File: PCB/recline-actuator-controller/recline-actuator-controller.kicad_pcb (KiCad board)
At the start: 4 copper layers, 140 x 100 mm, 130 parts, among them J1 DX07S016JA1R1500, J10 1757242, J11 1757242, J12 0705530002, J13 0705530002, J14 0705530002, J15 0705530002, J2 Conn_01x03, J3 RJHSE-5381, J4 1757242, J5 1757242, J6 1757242, J7 1757242, J8 1757242, J9 1757242, M1 D24V22F5, M2 D24V22F3, Q1 PSMN7R0-60YS,115, Q2 PSMN7R0-60YS,115, Q3 PSMN7R0-60YS,115, Q4 PSMN7R0-60YS,115, Q5 PSMN7R0-60YS,115, Q6 BSC014N04LSIATMA1, Q7 BSC014N04LSIATMA1, SW1 TL3330AF260QG, SW2 TL3330AF260QG, U1 TEMPLATE, U2 RP2040, U3 MAX3535ECWI+T, U4 VNH5019ATR-E, U5 VNH5019ATR-E, X1 ABM8G-12.000MHZ-18-D2Y-T

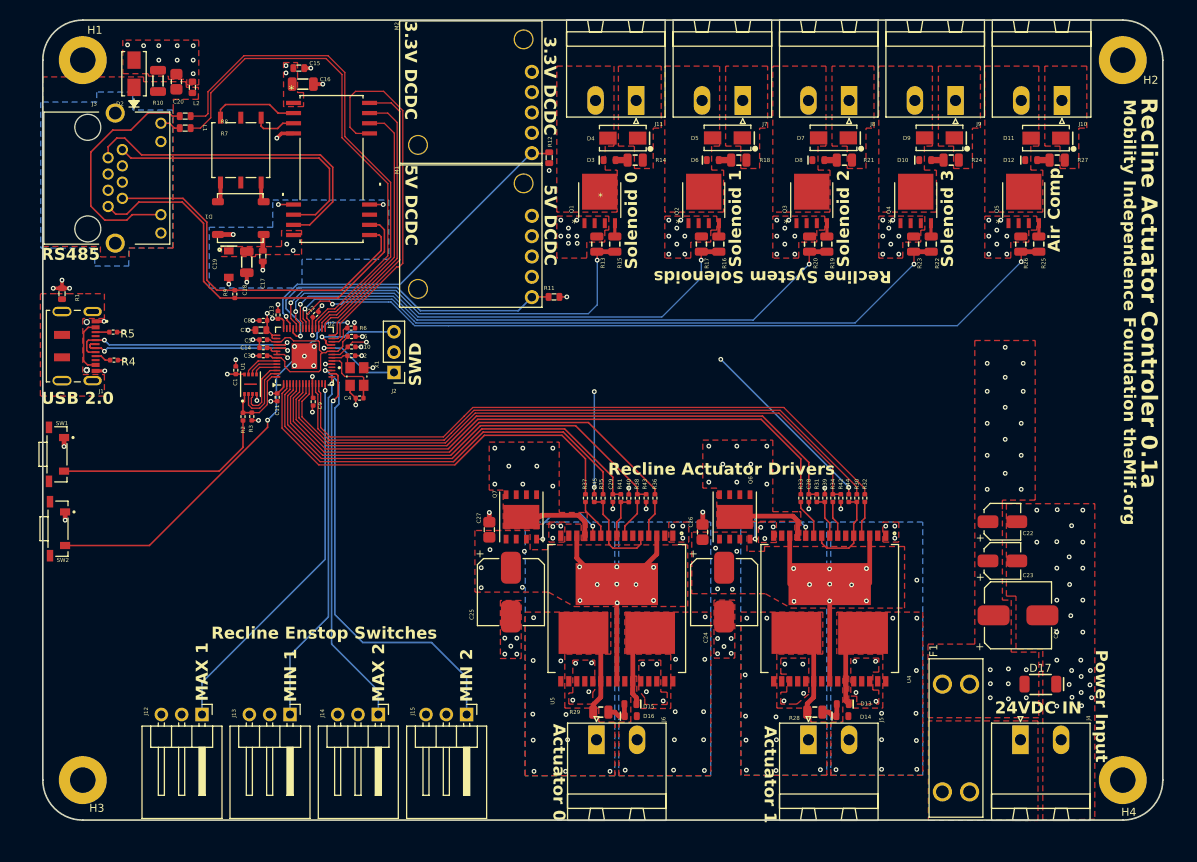
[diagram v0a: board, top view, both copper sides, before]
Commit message: More Motor Channels
Adding more motor channels to actuator control board it will need new MCU or port expansion.
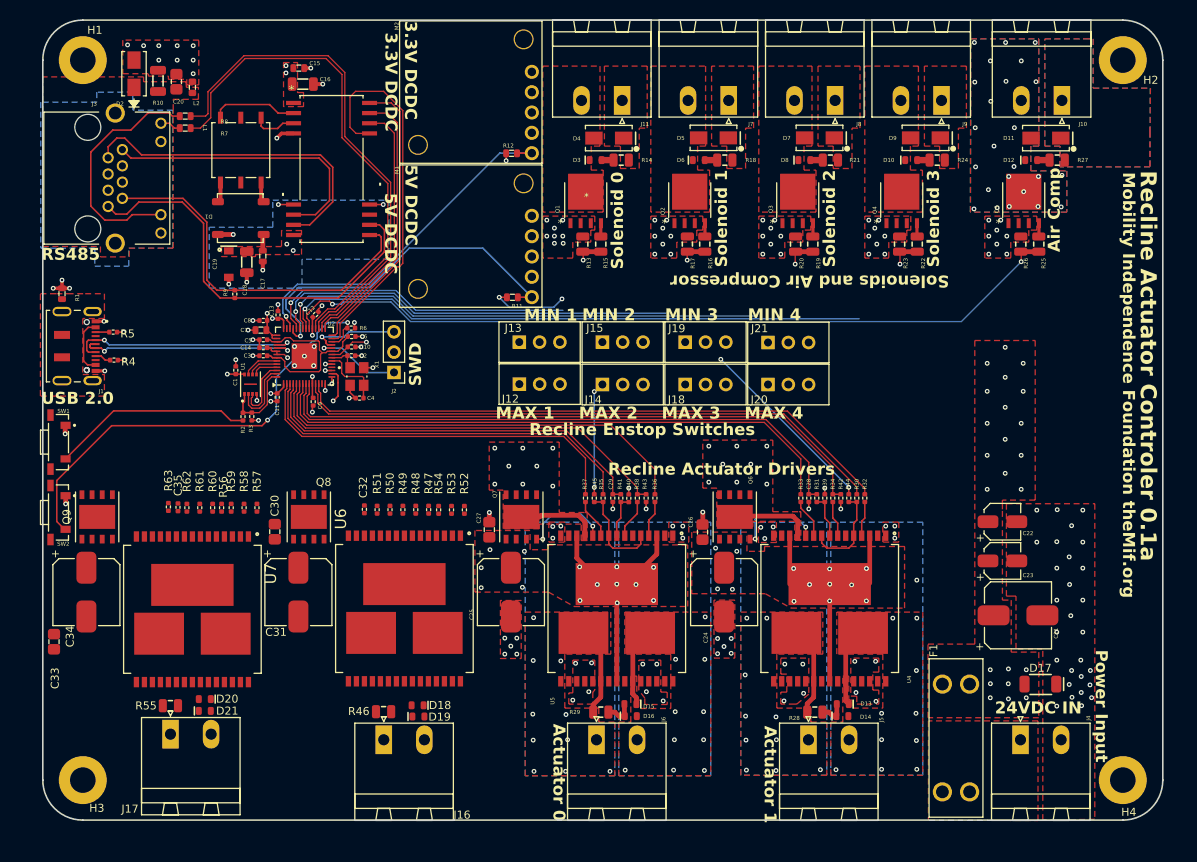
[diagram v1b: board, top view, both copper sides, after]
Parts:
- added C30: CL21B104KBFNNNE, AVR-KiCAD-Lib-Capacitors:C0805, F.Cu at (79.0, 109.0)
- added C31: UUQ1H470MCL1GS, AVR-KiCAD-Lib-Capacitors:CP_Elec_8x10, F.Cu at (82.0, 116.5)
- added C32: C0402C333K4REC7867, AVR-KiCAD-Lib-Capacitors:C0402, F.Cu at (90.2, 106.2)
- added C33: CL21B104KBFNNNE, AVR-KiCAD-Lib-Capacitors:C0805, F.Cu at (51.4, 122.7)
- added C34: UUQ1H470MCL1GS, AVR-KiCAD-Lib-Capacitors:CP_Elec_8x10, F.Cu at (55.5, 116.5)
- added C35: C0402C333K4REC7867, AVR-KiCAD-Lib-Capacitors:C0402, F.Cu at (66.9, 105.9)
- added D18: LTST-C194KGKT, AVR-KiCAD-Lib-Diodes:LED0603, F.Cu at (96.8, 130.7)
- added D19: LTST-C194TBKT, AVR-KiCAD-Lib-Diodes:LED0603, F.Cu at (97.0, 132.1)
- added D20: LTST-C194KGKT, AVR-KiCAD-Lib-Diodes:LED0603, F.Cu at (70.2, 129.9)
- added D21: LTST-C194TBKT, AVR-KiCAD-Lib-Diodes:LED0603, F.Cu at (70.2, 131.3)
- added J16: 1757242, AVR-KiCAD-Lib-Connectors:PhoenixContact_MSTBA-G_02x5.08mm_Angled, F.Cu at (92.6, 135.0)
- added J17: 1757242, AVR-KiCAD-Lib-Connectors:PhoenixContact_MSTBA-G_02x5.08mm_Angled, F.Cu at (66.0, 134.3)
- added J18: 0705430002, AVR-KiCAD-Lib-Connectors:Shrouded_Pin_Header_Straight_1x03_Pitch2.54mm, F.Cu at (130.3, 90.5)
- added J19: 0705430002, AVR-KiCAD-Lib-Connectors:Shrouded_Pin_Header_Straight_1x03_Pitch2.54mm, F.Cu at (130.3, 85.2)
- added J20: 0705430002, AVR-KiCAD-Lib-Connectors:Shrouded_Pin_Header_Straight_1x03_Pitch2.54mm, F.Cu at (140.7, 90.5)
- added J21: 0705430002, AVR-KiCAD-Lib-Connectors:Shrouded_Pin_Header_Straight_1x03_Pitch2.54mm, F.Cu at (140.7, 85.3)
- added Q8: BSC014N04LSIATMA1, AVR-KiCAD-Lib-Transistors:PG-TDSON-8_INF, F.Cu at (83.3, 107.1)
- added Q9: BSC014N04LSIATMA1, AVR-KiCAD-Lib-Transistors:PG-TDSON-8_INF, F.Cu at (56.8, 107.1)
- added R46: RC0805FR-074K7L, AVR-KiCAD-Lib-Resistors:R0805, F.Cu at (92.6, 131.4)
- added R47: RC0402FR-074K7L, AVR-KiCAD-Lib-Resistors:R0402, F.Cu at (98.2, 106.2)
- added R48: RC0402FR-071KL, AVR-KiCAD-Lib-Resistors:R0402, F.Cu at (96.6, 106.2)
- added R49: RC0402FR-071KL, AVR-KiCAD-Lib-Resistors:R0402, F.Cu at (95.0, 106.2)
- added R50: RC0402FR-071KL, AVR-KiCAD-Lib-Resistors:R0402, F.Cu at (93.4, 106.2)
- added R51: RC0402FR-071KL, AVR-KiCAD-Lib-Resistors:R0402, F.Cu at (91.8, 106.2)
- added R52: RC0402FR-071KL, AVR-KiCAD-Lib-Resistors:R0402, F.Cu at (102.7, 106.2)
- added R53: RC0402FR-0710KL, AVR-KiCAD-Lib-Resistors:R0402, F.Cu at (101.1, 106.2)
- added R54: RC0402FR-0710KL, AVR-KiCAD-Lib-Resistors:R0402, F.Cu at (99.5, 106.2)
- added R55: RC0805FR-074K7L, AVR-KiCAD-Lib-Resistors:R0805, F.Cu at (66.0, 130.7)
- added R56: RC0402FR-074K7L, AVR-KiCAD-Lib-Resistors:R0402, F.Cu at (72.3, 106.0)
- added R57: RC0402FR-071KL, AVR-KiCAD-Lib-Resistors:R0402, F.Cu at (76.8, 106.0)
- added R58: RC0402FR-071KL, AVR-KiCAD-Lib-Resistors:R0402, F.Cu at (75.2, 106.0)
- added R59: RC0402FR-071KL, AVR-KiCAD-Lib-Resistors:R0402, F.Cu at (73.5, 106.0)
- added R60: RC0402FR-071KL, AVR-KiCAD-Lib-Resistors:R0402, F.Cu at (71.2, 106.0)
- added R61: RC0402FR-071KL, AVR-KiCAD-Lib-Resistors:R0402, F.Cu at (69.6, 106.0)
- added R62: RC0402FR-0710KL, AVR-KiCAD-Lib-Resistors:R0402, F.Cu at (68.0, 106.0)
- added R63: RC0402FR-0710KL, AVR-KiCAD-Lib-Resistors:R0402, F.Cu at (65.7, 105.8)
- added U6: VNH5019ATR-E, AVR-KiCAD-Lib-ICs:IC_VNH5019ATR-E, F.Cu at (95.2, 118.5)
- added U7: VNH5019ATR-E, AVR-KiCAD-Lib-ICs:IC_VNH5019ATR-E, F.Cu at (68.7, 118.7)
- D11, D4, D5, D7, D9: value SMA -> B240A-13-F
- D2: value SMASeries -> SMAJ30CA
- J12, J13, J14, J15: value 0705530002 -> 0705430002; footprint AVR-KiCAD-Lib-Connectors:Pin_Header_Angled_1x03_Pitch2.54mm -> AVR-KiCAD-Lib-Connectors:Shrouded_Pin_Header_Straight_1x03_Pitch2.54mm
- moved J12 57.3 mm to (109.6, 90.5), turned to 90 degrees
- moved J13 54.7 mm to (109.6, 85.2), turned to 90 degrees
- moved J14 49.9 mm to (120.0, 90.5), turned to 90 degrees
- moved J15 49.5 mm to (120.0, 85.2), turned to 90 degrees
- moved R11 5.20 mm to (108.7, 79.7), turned to 180 degrees
- moved R12 4.73 mm to (108.6, 61.6), turned to 180 degrees
- moved SW2 2.03 mm to (52.0, 106.5)
- moved D10 1.75 mm to (158.6, 62.5)
- moved D3 1.75 mm to (119.1, 62.5)
- moved D4 1.75 mm to (120.8, 59.8)
- moved D5 1.75 mm to (133.8, 59.7)
- moved D6 1.75 mm to (132.0, 62.5)
- moved D7 1.75 mm to (147.1, 59.7)
- moved D8 1.75 mm to (145.2, 62.5)
- moved D9 1.75 mm to (160.3, 59.7)
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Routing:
- net /End Stop Limit Switches/MIN2: track 56.7 -> 1.04 mm
- net /End Stop Limit Switches/MAX1: track 47.8 -> 0.86 mm
- net /End Stop Limit Switches/MIN1: track 44.4 -> 0.86 mm
- net /End Stop Limit Switches/MAX2: track 46.0 -> 4.28 mm
- net /RP2040/SOLENOID_0: track 53.0 -> 42.5 mm
- net /RP2040/SOLENOID_3: track 87.4 -> 77.3 mm
- net +3.3V: track 63.8 -> 73.6 mm, vias 18 -> 19
- net /RP2040/SOLENOID_2: track 75.2 -> 65.6 mm
- net /RP2040/SOLENOID_1: track 63.4 -> 54.5 mm
- net /Motor H-Bridges/M1ENA/B: track 80.1 -> 75.2 mm
- net /Motor H-Bridges/M1INA: track 80.5 -> 75.6 mm
- net /Motor H-Bridges/M1PWM: track 81.0 -> 76.7 mm
- net /Motor H-Bridges/M1CS: track 78.7 -> 74.5 mm
- net /Motor H-Bridges/M2ENA/B: track 53.6 -> 49.4 mm
- net /Motor H-Bridges/M2INB: track 52.8 -> 48.6 mm
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- added copper zone on B.Cu, net +24V
- added copper zone on B.Cu, net Net-(Q5-D)
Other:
- board text added: "MAX 3"
- board text added: "MAX 4"
- board text added: "MIN 3"
- board text added: "MIN 4"
- board text added: "Solenoids and Air Compressor"
- board text removed: "Recline System Solenoids"

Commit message: Recline Actuator Board Redesign
Recline actuator control board redesign complete, functionality extended to handle two additional large actuators for leg lifting. Air compressor switching circuit made to handle higher current. Additional end stops for additional actuators added, IO expander added for more input to RP2040. Current sensing for all 4 actuators.
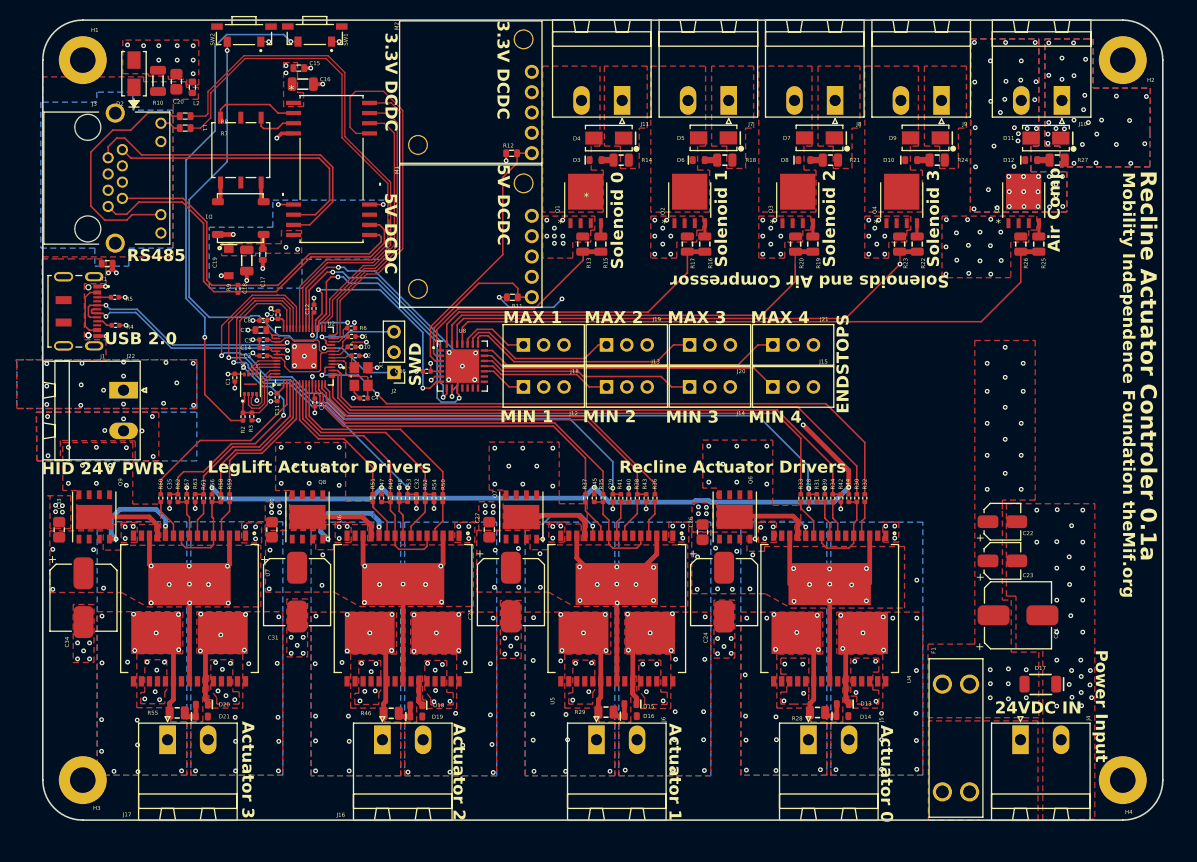
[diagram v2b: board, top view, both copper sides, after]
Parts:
- added C36: C0402C104K9PACTU, AVR-KiCAD-Lib-Resistors:R0402, F.Cu at (98.0, 88.9)
- added J22: 1757242, AVR-KiCAD-Lib-Connectors:PhoenixContact_MSTBA-G_02x5.08mm_Angled, F.Cu at (60.1, 91.3)
- added U8: MCP23S17T-E/ML, AVR-KiCAD-Lib-ICs:QFN28_6x6MC_MCH-L, F.Cu at (102.5, 88.2)
- moved SW2 64.1 mm to (75.2, 46.8), turned to 180 degrees
- moved SW1 60.2 mm to (84.0, 46.8), turned to 180 degrees
- moved J15 22.0 mm to (141.2, 90.8)
- moved J18 20.8 mm to (110.1, 85.6)
- moved C33 14.0 mm to (52.0, 108.7), turned to -90 degrees
- moved J13 12.3 mm to (120.5, 90.8)
- moved J20 11.0 mm to (130.9, 85.6)
- moved J14 10.9 mm to (130.8, 90.8)
- moved J19 9.85 mm to (120.5, 85.6)
- moved R57 8.85 mm to (68.0, 104.8)
- moved R1 6.78 mm to (58.0, 75.5), turned to 0 degrees
- moved R50 6.76 mm to (100.0, 104.8), turned to 90 degrees
- moved C32 6.65 mm to (96.7, 104.8)
- moved R60 6.59 mm to (64.8, 104.8), turned to 90 degrees
- moved R47 6.06 mm to (92.3, 104.8), turned to 90 degrees
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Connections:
- J12 pad 1: /End Stop Limit Switches/MAX1 -> /End Stop Limit Switches/MIN1
- J13 pad 1: /End Stop Limit Switches/MIN1 -> /End Stop Limit Switches/MIN2
- J14 pad 1: /End Stop Limit Switches/MAX2 -> /End Stop Limit Switches/MIN3
- J15 pad 1: /End Stop Limit Switches/MIN2 -> /End Stop Limit Switches/MIN4
- J18 pad 1: /End Stop Limit Switches/MAX3 -> /End Stop Limit Switches/MAX1
- J19 pad 1: /End Stop Limit Switches/MIN3 -> /End Stop Limit Switches/MAX2
- J20 pad 1: /End Stop Limit Switches/MAX4 -> /End Stop Limit Switches/MAX3
- J21 pad 1: /End Stop Limit Switches/MIN4 -> /End Stop Limit Switches/MAX4
- R13 pad 1: /RP2040/SOLENOID_0 -> /End Stop Limit Switches/SOLENOID_0
- R15 pad 1: /RP2040/SOLENOID_0 -> /End Stop Limit Switches/SOLENOID_0
- R16 pad 1: /RP2040/SOLENOID_1 -> /End Stop Limit Switches/SOLENOID_1
- R17 pad 1: /RP2040/SOLENOID_1 -> /End Stop Limit Switches/SOLENOID_1
- R19 pad 1: /RP2040/SOLENOID_2 -> /End Stop Limit Switches/SOLENOID_2
- R20 pad 1: /RP2040/SOLENOID_2 -> /End Stop Limit Switches/SOLENOID_2
- R22 pad 1: /RP2040/SOLENOID_3 -> /End Stop Limit Switches/SOLENOID_3
- R23 pad 1: /RP2040/SOLENOID_3 -> /End Stop Limit Switches/SOLENOID_3
- R25 pad 1: /RP2040/AIR_COMP -> /End Stop Limit Switches/AIR_COMP
- R26 pad 1: /RP2040/AIR_COMP -> /End Stop Limit Switches/AIR_COMP
- U2 pad 11: /Motor H-Bridges/M1ENA/B -> /Motor H-Bridges/M2INB
- U2 pad 12: /Motor H-Bridges/M1INA -> /Motor H-Bridges/M2ENA/B
- U2 pad 13: unconnected-(U2-GPIO10-Pad13) -> /Motor H-Bridges/M2PWM
- U2 pad 14: /End Stop Limit Switches/MAX1 -> /Motor H-Bridges/M2INA
- U2 pad 15: /End Stop Limit Switches/MIN1 -> /Motor H-Bridges/M1INB
- U2 pad 16: /End Stop Limit Switches/MAX2 -> /Motor H-Bridges/M1PWM
- U2 pad 17: /End Stop Limit Switches/MIN2 -> /Motor H-Bridges/M1ENA/B
- U2 pad 18: unconnected-(U2-GPIO15-Pad18) -> /Motor H-Bridges/M1INA
- U2 pad 2: /Motor H-Bridges/M2INB -> /Leg Lift Motors/M4INB
- U2 pad 3: /Motor H-Bridges/M2ENA/B -> /Leg Lift Motors/M4PWM
- U2 pad 31: /RP2040/RS485_RX_LED -> /RP2040/SPI0_RX
- U2 pad 32: /RP2040/RS485_TX_LED -> /RP2040/SPI0_CSn
- U2 pad 34: /RP2040/AIR_COMP -> /RP2040/SPI0_SCK
- U2 pad 35: /RP2040/SOLENOID_3 -> /RP2040/SPI0_TX
- U2 pad 36: /RP2040/SOLENOID_2 -> /RP2040/RS485_RX_LED
- U2 pad 37: /RP2040/SOLENOID_1 -> /RP2040/RS485_TX_LED
- U2 pad 38: /RP2040/SOLENOID_0 -> /Motor H-Bridges/M1CS
- U2 pad 39: /Power/5V_PG -> /Motor H-Bridges/M2CS
- U2 pad 4: /Motor H-Bridges/M2CS -> /Leg Lift Motors/M4ENA/B
- U2 pad 40: /Power/3.3V_PG -> /Leg Lift Motors/M3CS
- U2 pad 41: unconnected-(U2-GPIO29_ADC3-Pad41) -> /Leg Lift Motors/M4CS
- U2 pad 5: /Motor H-Bridges/M2PWM -> /Leg Lift Motors/M4INA
- U2 pad 6: /Motor H-Bridges/M2INA -> /Leg Lift Motors/M3INB
- U2 pad 7: /Motor H-Bridges/M1INB -> /Leg Lift Motors/M3ENA/B
- U2 pad 8: /Motor H-Bridges/M1CS -> /Leg Lift Motors/M3PWM
- U2 pad 9: /Motor H-Bridges/M1PWM -> /Leg Lift Motors/M3INA
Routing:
- net /RP2040/AIR_COMP: track 99.8 -> 0.00 mm, vias 2 -> 0
- net /End Stop Limit Switches/AIR_COMP: track 0.00 -> 80.4 mm
- net /RP2040/SOLENOID_3: track 77.3 -> 0.00 mm, vias 2 -> 0
- net /RP2040/SOLENOID_2: track 65.6 -> 0.00 mm, vias 2 -> 0
- net /End Stop Limit Switches/SOLENOID_3: track 0.00 -> 64.7 mm, vias 0 -> 1
- net +3.3V: track 73.6 -> 137.3 mm, vias 19 -> 21
- net /RP2040/SOLENOID_1: track 54.5 -> 0.00 mm, vias 2 -> 0
- net /End Stop Limit Switches/SOLENOID_2: track 0.00 -> 53.5 mm
- net /Leg Lift Motors/M3CS: track 0.00 -> 46.4 mm, vias 0 -> 2
- net /Leg Lift Motors/M4CS: track 0.00 -> 43.7 mm, vias 0 -> 2
- net /RP2040/SOLENOID_0: track 42.5 -> 0.00 mm, vias 2 -> 0
- net /End Stop Limit Switches/SOLENOID_1: track 0.00 -> 40.1 mm
- net Net-(R2-Pad1): track 25.2 -> 63.5 mm, vias 0 -> 2
- net /End Stop Limit Switches/MAX4: track 0.00 -> 37.8 mm
- net /End Stop Limit Switches/MIN4: track 0.00 -> 37.7 mm
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- added copper zone on In1.Cu, net +24V
- added copper zone on B.Cu, net /Leg Lift Motors/M3OUTA
- added copper zone on F.Cu, net /Leg Lift Motors/M3OUTA
- added copper zone on In2.Cu, net /Leg Lift Motors/M3OUTA
- added copper zone on B.Cu, net /Leg Lift Motors/M3OUTB
- added copper zone on F.Cu, net /Leg Lift Motors/M3OUTB
- added copper zone on In2.Cu, net /Leg Lift Motors/M3OUTB
- added copper zone on B.Cu, net /Leg Lift Motors/M4OUTA
- added copper zone on F.Cu, net /Leg Lift Motors/M4OUTA
- added copper zone on In2.Cu, net /Leg Lift Motors/M4OUTA
- added copper zone on B.Cu, net /Leg Lift Motors/M4OUTB
- added copper zone on F.Cu, net /Leg Lift Motors/M4OUTB
- added copper zone on In2.Cu, net /Leg Lift Motors/M4OUTB
- added copper zone on F.Cu, net /Leg Lift Motors/VMOT3
- added copper zone on In2.Cu, net /Leg Lift Motors/VMOT3
- added copper zone on F.Cu, net /Leg Lift Motors/VMOT4
- added copper zone on In2.Cu, net /Leg Lift Motors/VMOT4
- added copper zone on B.Cu, net GND
- added copper zone on In1.Cu, net Net-(Q5-D)
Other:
- board text added: "Actuator 2"
- board text added: "Actuator 3"
- board text added: "ENDSTOPS"
- board text added: "HID 24V PWR"
- board text added: "LegLift Actuator Drivers"
- board text removed: "Recline Enstop Switches"
